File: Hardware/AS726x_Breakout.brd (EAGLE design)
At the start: 25.4 x 25.4 mm, 25 parts, among them J2 Serial Interface, U1 AS726X, U3 4MB Flash

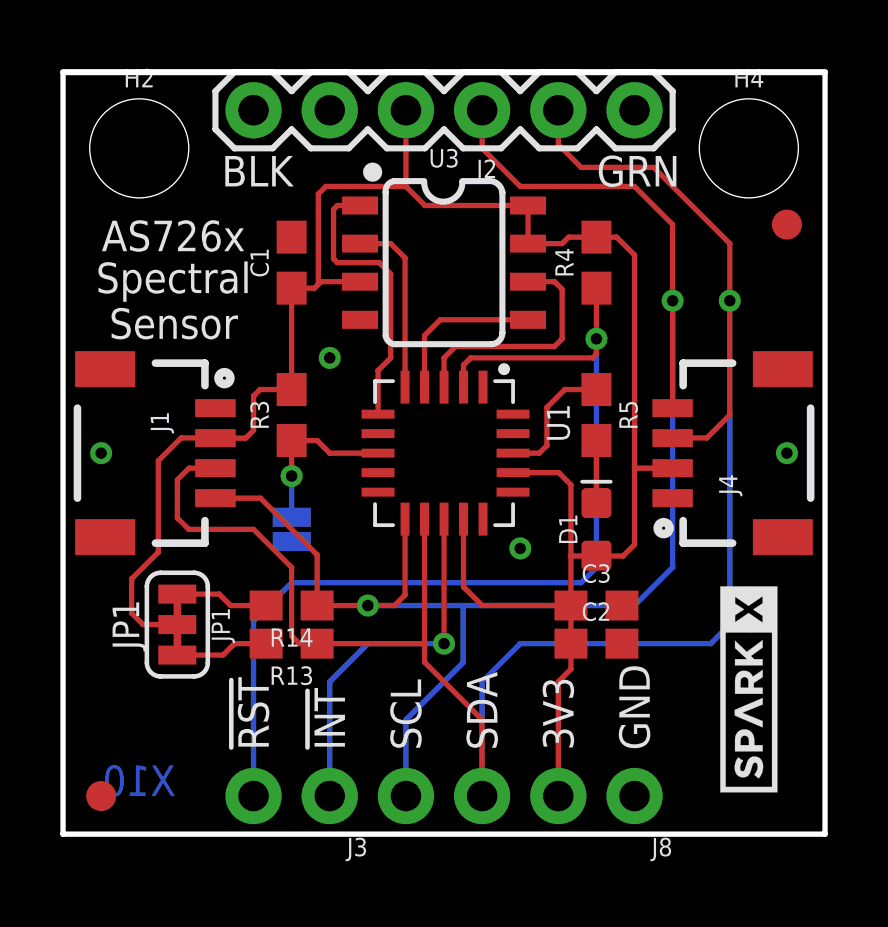
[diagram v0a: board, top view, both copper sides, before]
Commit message: Adding firmware, panel, and small fix to dimension on main layout.
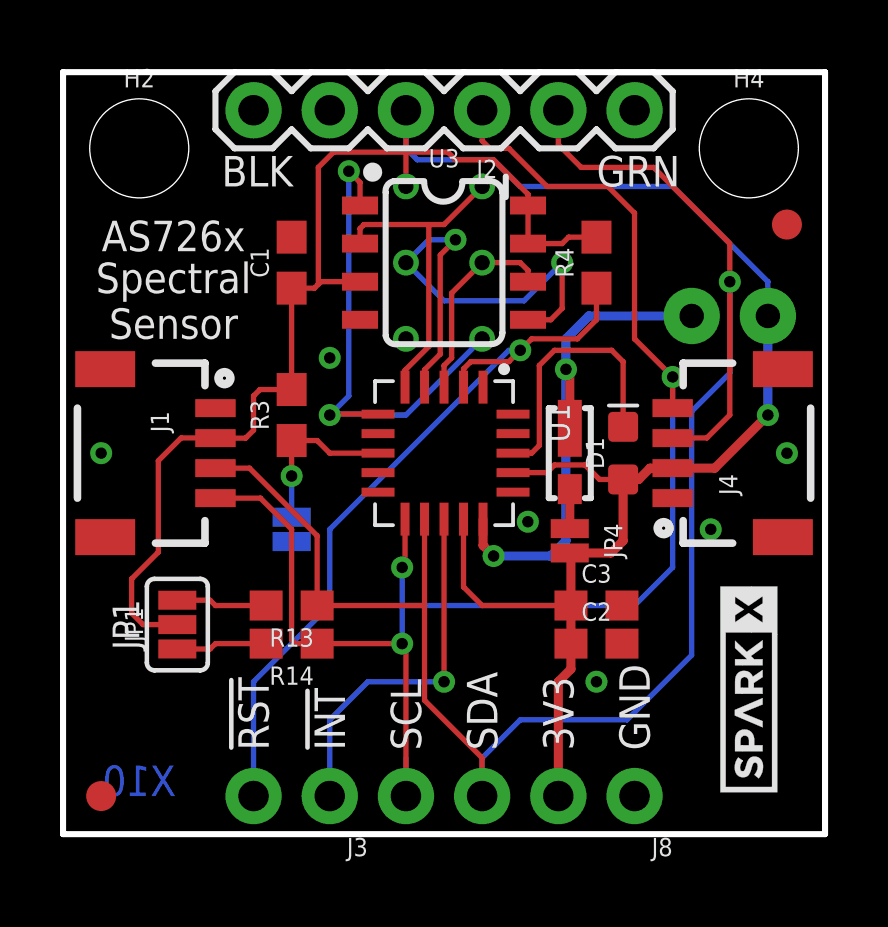
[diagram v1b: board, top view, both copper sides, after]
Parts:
- removed R5: 0, SparkFun-Resistors:0603
- added D2: 5700k, SparkX:SUPER_BRIGHT_SMD_LED_1206
- added D4: Incandescent, SparkX:LED_5MM_NOSILK
- added J5: Flash Programming, SparkFun-Connectors:2X3_TEST_POINTS
- added JP4: (no value), SparkFun-Jumpers:SMT-JUMPER_2_NC_PASTE_NO-SILK
- JP1: device SparkFun-Jumpers:SMT-JUMPER_3_2-NC_TRACE_SILK -> SparkFun-Jumpers:SMT-JUMPER_3_2-NC_PASTE_SILK
- moved D1 2.69 mm to (18.7, 12.7)
- moved R13 1.27 mm to (7.62, 7.62)
- moved R14 1.27 mm to (7.62, 6.35)
- turned JP1 to 90 degrees
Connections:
- removed net N$3: D1.C, R5.2
- new net LED_DRV: D2.C, D4.K, U1.15
- net !CS_EE: now also J5.5
- net 3.3V: now also D4.A, J5.2, JP4.2
- net GND: now also J5.6
- net MISO: now also J5.1
- net MOSI: now also J5.4
- net N$2: now also D1.C; no longer R5.1
- net N$6: now also D2.A, JP4.1; no longer U1.15
- net SCK: now also J5.3
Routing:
- net LED_DRV: track 0.00 -> 17.3 mm, vias 0 -> 2
- net 3.3V: track 69.0 -> 84.9 mm, vias 0 -> 1
- net MOSI: track 5.39 -> 16.4 mm, vias 0 -> 2
- net !CS_EE: track 9.55 -> 17.5 mm, vias 0 -> 2
- net !RST: track 33.1 -> 25.5 mm
- net MISO: track 6.00 -> 10.9 mm
- net TX/SDA: track 63.9 -> 59.1 mm
- net N$2: track 4.40 -> 8.98 mm
- net N$3: track 2.08 -> 0.00 mm
- net RX/SCL: track 53.0 -> 51.0 mm, vias 2 -> 3
- net SCK: track 8.07 -> 6.69 mm
- net N$6: track 0.00 -> 1.31 mm
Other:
- board text added: "7262-Vis"
- board text added: "7263-IR"
- board text added: "Bulb"
- board text added: "I2C"
- board text added: "Serial"

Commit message: Examples are fully functional
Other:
- board text added: "5700K"
